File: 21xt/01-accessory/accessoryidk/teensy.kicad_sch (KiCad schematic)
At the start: 14 parts, among them T1 749013011, U3 DEV-16771

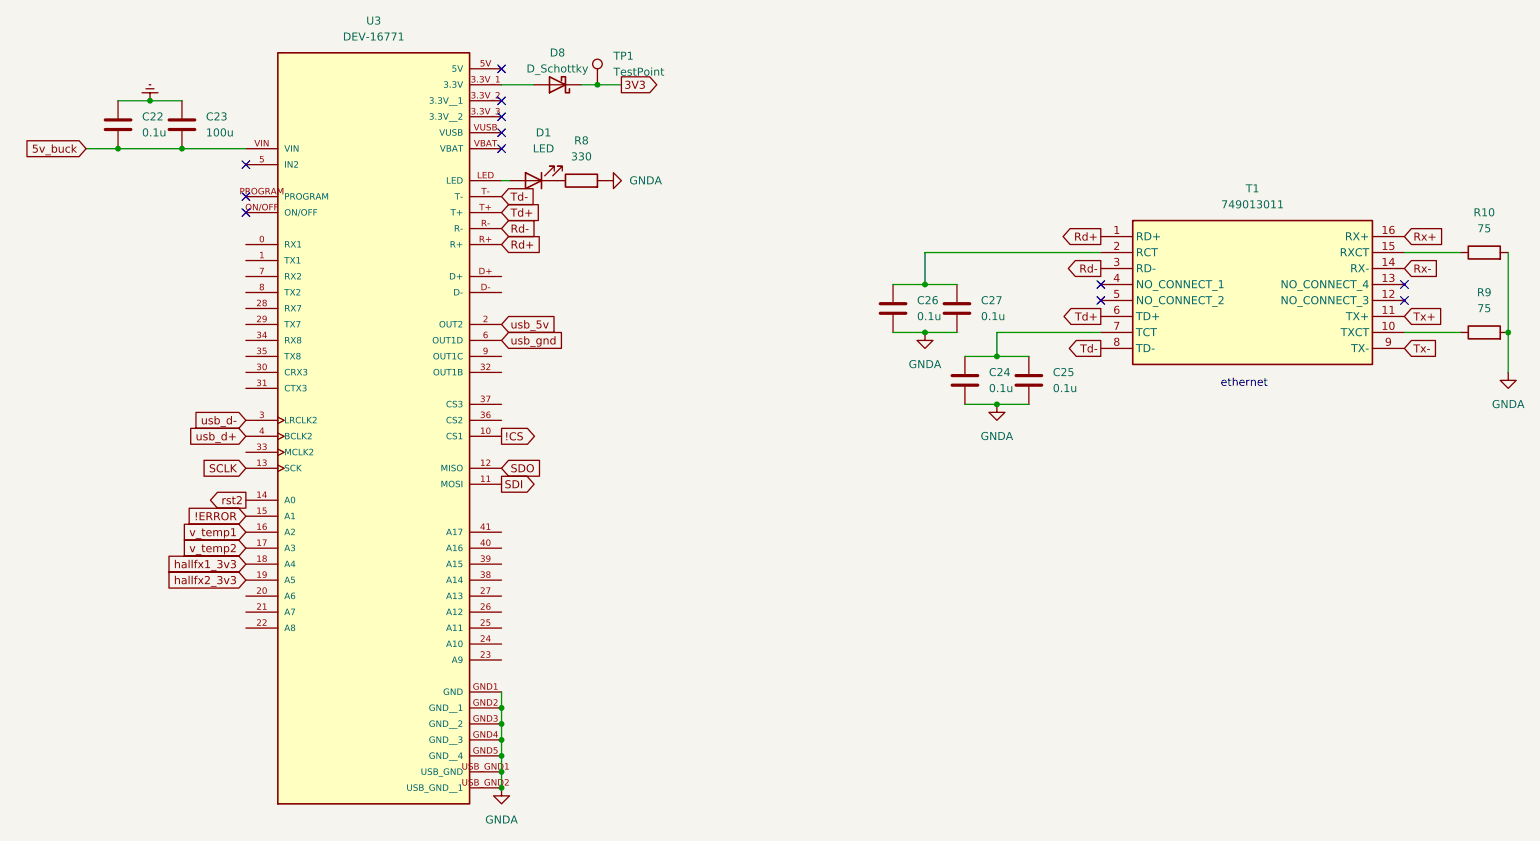
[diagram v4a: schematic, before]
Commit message: Finished Accessory V1 schematic, need DRC checks
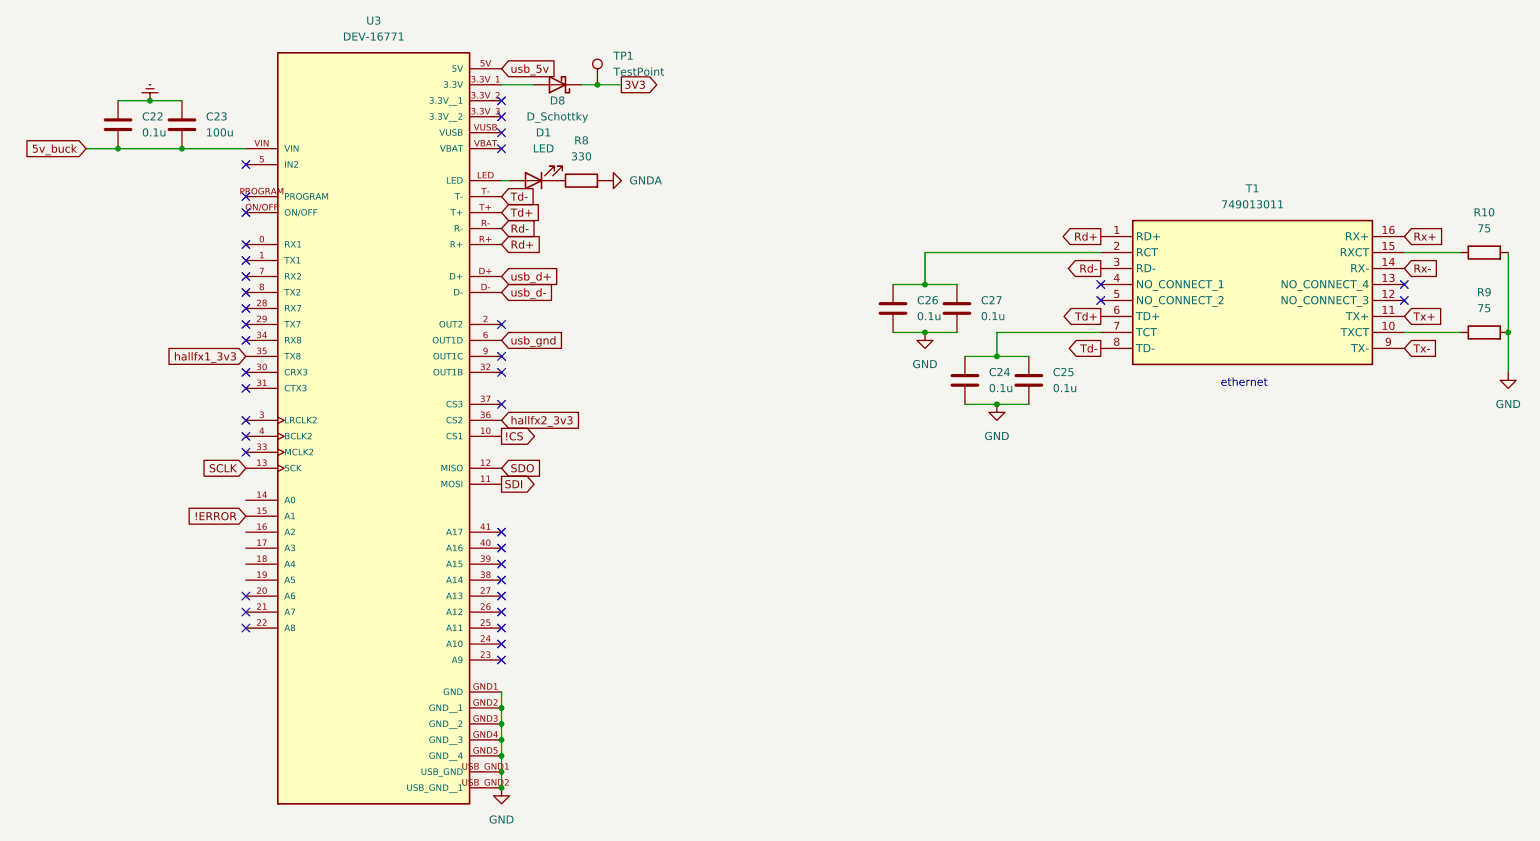
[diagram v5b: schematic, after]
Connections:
- net GNDA: no longer C24.2, C25.2, C26.2, C27.2, R10.2, R9.2, U3.GND1 (GND), U3.GND2 (GND__1), U3.GND3 (GND__2), U3.GND4 (GND__3), U3.GND5 (GND__4), U3.USB_GND1 (USB_GND), U3.USB_GND2 (USB_GND__1)
- net hallfx1_3v3: now also U3.35 (TX8); no longer U3.18 (A4)
- net hallfx2_3v3: now also U3.36 (CS2); no longer U3.19 (A5)
- net usb_5v: now also U3.5V; no longer U3.2 (OUT2)
- net usb_d+: now also U3.D+; no longer U3.4 (BCLK2)
- net usb_d-: now also U3.D-; no longer U3.3 (LRCLK2)
- net rst2: no longer names the net of U3.14 (A0)
- net v_temp1: no longer names the net of U3.16 (A2)
- net v_temp2: no longer names the net of U3.17 (A3)
- new net GND: C24.2, C25.2, C26.2, C27.2, R10.2, R9.2, U3.GND1 (GND), U3.GND2 (GND__1), U3.GND3 (GND__2), U3.GND4 (GND__3), U3.GND5 (GND__4), U3.USB_GND1 (USB_GND), U3.USB_GND2 (USB_GND__1)
- no-connect marks 12 -> 39

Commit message: Revising accessory schematic
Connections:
- net usb_5v: no longer names the net of U3.5V
- no-connect marks 39 -> 40
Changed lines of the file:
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@@
   (no_connect (at 116.84 124.46))
   (no_connect (at 116.84 121.92))
+  (no_connect (at 116.84 43.18))
   (no_connect (at 76.2 129.54))
   (no_connect (at 212.09 77.47))
@@
     )
   )
-  (global_label "usb_5v" (shape input) (at 116.84 43.18 0) (fields_autoplaced)
-    (effects (font (size 1.27 1.27)) (justify left))
-    (property "Intersheetrefs" "${INTERSHEET_REFS}" (at 126.296 43.18 0)
-      (effects (font (size 1.27 1.27)) (justify left) hide)
-    )
-  )

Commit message: Editing V1 accessory layout
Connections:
- net GND is gone; now on net GND1: C24.2, C25.2, C26.2, C27.2, R10.2, R9.2, U3.GND1 (GND), U3.GND2 (GND__1), U3.GND3 (GND__2), U3.GND4 (GND__3), U3.GND5 (GND__4), U3.USB_GND1 (USB_GND), U3.USB_GND2 (USB_GND__1)
- net GNDA is gone; now on net GND1: R8.2
- net Earth renamed GND1

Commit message: FINISHED accessory edited v1 layout, need to check silkscreen
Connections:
- net hallfx1_3v3: now also U3.17 (A3); no longer U3.35 (TX8)
- net hallfx2_3v3: now also U3.16 (A2); no longer U3.36 (CS2)
- no-connect marks 40 -> 45
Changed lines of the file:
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@@
   (no_connect (at 76.2 66.04))
   (no_connect (at 116.84 119.38))
+  (no_connect (at 76.2 124.46))
   (no_connect (at 76.2 132.08))
   (no_connect (at 76.2 58.42))
@@
   (no_connect (at 116.84 116.84))
   (no_connect (at 76.2 99.06))
+  (no_connect (at 76.2 88.9))
   (no_connect (at 76.2 63.5))
   (no_connect (at 76.2 76.2))
@@
   (no_connect (at 76.2 73.66))
   (no_connect (at 116.84 96.52))
+  (no_connect (at 116.84 99.06))
+  (no_connect (at 76.2 111.76))
   (no_connect (at 76.2 81.28))
+  (no_connect (at 76.2 121.92))
   (no_connect (at 76.2 93.98))
   (no_connect (at 116.84 129.54))
@@
     )
   )
-  (global_label "hallfx2_3v3" (shape input) (at 116.84 99.06 0) (fields_autoplaced)
-    (effects (font (size 1.27 1.27)) (justify left))
-    (property "Intersheetrefs" "${INTERSHEET_REFS}" (at 130.7711 99.06 0)
-      (effects (font (size 1.27 1.27)) (justify left) hide)
-    )
-  )
   (global_label "Rd-" (shape output) (at 212.09 74.93 180) (fields_autoplaced)
     (effects (font (size 1.27 1.27)) (justify right))
@@
     )
   )
+  (global_label "hallfx2_3v3" (shape input) (at 76.2 116.84 180) (fields_autoplaced)
+    (effects (font (size 1.27 1.27)) (justify right))
+    (property "Intersheetrefs" "${INTERSHEET_REFS}" (at 62.2689 116.84 0)
+      (effects (font (size 1.27 1.27)) (justify right) hide)
+    )
+  )
   (global_label "usb_d-" (shape input) (at 116.84 78.74 0) (fields_autoplaced)
     (effects (font (size 1.27 1.27)) (justify left))
@@
     )
   )
+  (global_label "hallfx1_3v3" (shape input) (at 76.2 119.38 180) (fields_autoplaced)
+    (effects (font (size 1.27 1.27)) (justify right))
+    (property "Intersheetrefs" "${INTERSHEET_REFS}" (at 62.2689 119.38 0)
+      (effects (font (size 1.27 1.27)) (justify right) hide)
+    )
+  )
   (global_label "Td-" (shape input) (at 116.84 63.5 0) (fields_autoplaced)
     (effects (font (size 1.27 1.27)) (justify left))
@@
       (effects (font (size 1.27 1.27)) (justify right) hide)
     )
-  )
-  (global_label "hallfx1_3v3" (shape input) (at 76.2 88.9 180) (fields_autoplaced)
-    (effects (font (size 1.27 1.27)) (justify right))
-    (property "Intersheetrefs" "${INTERSHEET_REFS}" (at 62.2689 88.9 0)
-      (effects (font (size 1.27 1.27)) (justify right) hide)
-    )
